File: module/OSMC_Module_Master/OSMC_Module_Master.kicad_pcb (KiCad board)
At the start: 4 copper layers, 34 x 41 mm, 10 parts, among them SW1 SW_Push, SW2 SW_Push, SW3 SW_Push, U1 OSMC Module Board w/pins, U2 24LC02BT-I/OT, U3 PCF8574DWR

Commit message: reviewed PCBs
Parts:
- added J1: SolderJumper_2_Bridged, Jumper:SolderJumper-2_P1.3mm_Bridged2Bar_Pad1.0x1.5mm, B.Cu at (186.4, 71.3)
- added J2: SolderJumper_2_Bridged, Jumper:SolderJumper-2_P1.3mm_Bridged2Bar_Pad1.0x1.5mm, B.Cu at (188.3, 69.5)
- added J3: SolderJumper_2_Bridged, Jumper:SolderJumper-2_P1.3mm_Bridged2Bar_Pad1.0x1.5mm, B.Cu at (190.1, 67.6)
- D1, D2, D3, D4: footprint LED_THT:LED_D5.0mm -> LED_SMD:LED_0603_1608Metric_Pad1.05x0.95mm_HandSolder
- moved D3 7.50 mm to (208.2, 75.8)
- moved D4 6.73 mm to (208.2, 80.8)
- moved D2 3.60 mm to (185.7, 80.8)
- moved D1 3.29 mm to (185.7, 75.8)
- moved U3 0.70 mm to (197.0, 76.4)
- moved U1 0.69 mm to (197.0, 76.4)
- moved SW3 0.16 mm to (201.1, 86.9)
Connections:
- D1 pad 1: GND -> /3v3
- D2 pad 1: GND -> /3v3
- D3 pad 1: GND -> /3v3
- D4 pad 1: GND -> /3v3
- U1 pad 18: unconnected-(U1-A3-Pad18) -> /A2
- U1 pad 19: unconnected-(U1-A2-Pad19) -> /A1
- U1 pad 20: unconnected-(U1-A1-Pad20) -> /A0
- U3 pad 1: GND -> /A0
- U3 pad 16: /5V -> /3v3
- U3 pad 2: GND -> /A1
- U3 pad 3: GND -> /A2
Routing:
- net /3v3: track 71.8 -> 13.7 mm, vias 2 -> 8
- net unconnected-(U1-PadMP)_3: track 30.1 -> 0.00 mm, vias 2 -> 0
- net /A2: track 0.00 -> 28.6 mm, vias 0 -> 1
- net /A1: track 0.00 -> 27.2 mm, vias 0 -> 1
- net /A0: track 0.00 -> 25.7 mm, vias 0 -> 1
- net /5V: track 47.5 -> 31.2 mm, vias 0 -> 1
- net /D4: track 22.6 -> 14.8 mm
- net /B2: track 30.8 -> 24.9 mm
- net /SCL: track 51.3 -> 45.6 mm, vias 2 -> 0
- net /SDA: track 49.3 -> 44.9 mm, vias 3 -> 2
- net /INT: track 48.4 -> 45.4 mm, vias 1 -> 3
- net /D2: track 9.50 -> 6.96 mm, vias 0 -> 1
- net /D1: track 8.09 -> 6.49 mm, vias 0 -> 1
- net GND: track 16.2 -> 17.4 mm, vias 7 -> 5
- net /D3: track 18.0 -> 17.2 mm, vias 0 -> 1
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- added copper zone on In2.Cu, net /3v3

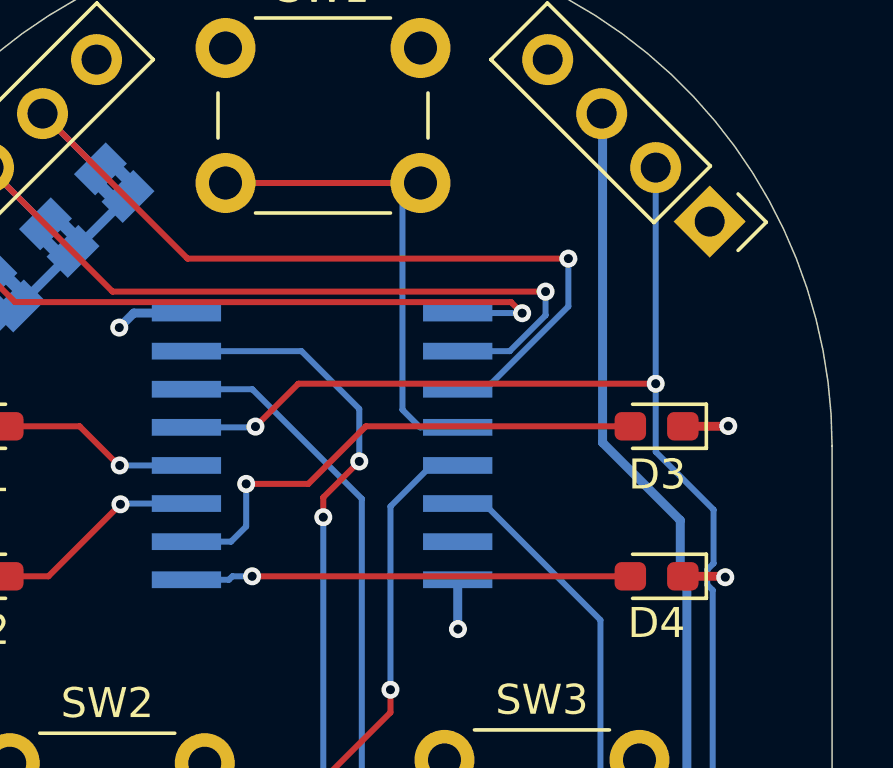
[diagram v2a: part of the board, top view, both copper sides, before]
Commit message: update to modules gerbers produced
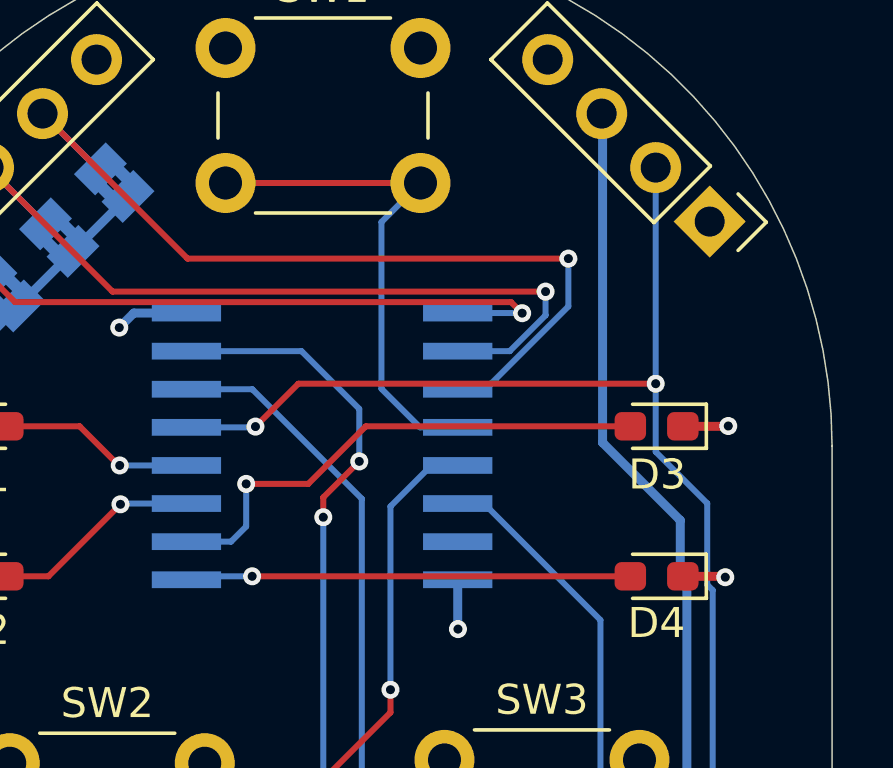
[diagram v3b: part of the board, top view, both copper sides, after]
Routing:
- net /B1: track 16.4 -> 17.0 mm
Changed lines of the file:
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@@
-	)
-	(segment
-		(start 210.06 78.55)
-		(end 208.130812 76.620812)
-		(width 0.2)
-		(layer "B.Cu")
-		(net 9)
 	)
 	(segment
@@
 	)
 	(segment
-		(start 210.06 80.340057)
-		(end 210.06 78.55)
+		(start 208.130812 76.620812)
+		(end 208.130812 74.35)
 		(width 0.2)
 		(layer "B.Cu")
@@
 	)
 	(segment
-		(start 209.849 80.551057)
-		(end 210.06 80.340057)
-		(width 0.2)
-		(layer "B.Cu")
-		(net 9)
-	)
-	(segment
-		(start 208.130812 76.620812)
-		(end 208.130812 74.35)
+		(start 210.0306 81.230543)
+		(end 209.849 81.048943)
+		(width 0.2)
+		(layer "B.Cu")
+		(net 9)
+	)
+	(segment
+		(start 209.849 78.339)
+		(end 208.130812 76.620812)
 		(width 0.2)
 		(layer "B.Cu")
@@
 	)
 	(segment
-		(start 209.849 81.048943)
-		(end 209.849 80.551057)
-		(width 0.2)
-		(layer "B.Cu")
-		(net 9)
-	)
-	(segment
 		(start 210.0306 92.6994)
 		(end 210.0306 81.230543)
@@
 	)
 	(segment
-		(start 210.0306 81.230543)
-		(end 209.849 81.048943)
-		(width 0.2)
-		(layer "B.Cu")
-		(net 9)
-	)
-	(segment
 		(start 208.130812 74.35)
 		(end 208.130812 67.146115)
@@
 	)
 	(segment
+		(start 209.849 81.048943)
+		(end 209.849 78.339)
+		(width 0.2)
+		(layer "B.Cu")
+		(net 9)
+	)
+	(segment
 		(start 200.291 67.66)
 		(end 193.791 67.66)
@@
 	)
 	(segment
-		(start 200.291 67.66)
-		(end 199.69 68.261)
-		(width 0.2)
-		(layer "B.Cu")
-		(net 10)
-	)
-	(segment
 		(start 200.275 75.805)
 		(end 201.5312 75.805)
@@
 	)
 	(segment
-		(start 199.69 68.261)
-		(end 199.69 75.22)
-		(width 0.2)
-		(layer "B.Cu")
-		(net 10)
-	)
-	(segment
-		(start 199.69 75.22)
+		(start 200.291 67.66)
+		(end 198.99 68.961)
+		(width 0.2)
+		(layer "B.Cu")
+		(net 10)
+	)
+	(segment
+		(start 198.99 68.961)
+		(end 198.99 74.52)
+		(width 0.2)
+		(layer "B.Cu")
+		(net 10)
+	)
+	(segment
+		(start 198.99 74.52)
 		(end 200.275 75.805)
 		(width 0.2)
@@
 	(segment
 		(start 194.68 80.77)
-		(end 194.02 80.77)
+		(end 192.6038 80.77)
 		(width 0.2)
 		(layer "B.Cu")
@@
 	)
 	(segment
-		(start 193.905 80.885)
+		(start 192.6038 80.77)
 		(end 192.4888 80.885)
 		(width 0.2)
 		(layer "B.Cu")
-		(net 16)
-	)
-	(segment
-		(start 194.02 80.77)
-		(end 193.905 80.885)
-		(width 0.2)
-		(layer "B.Cu")

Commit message: created all gerber zips
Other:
- board text added: "BN MOD V1 2/26"
